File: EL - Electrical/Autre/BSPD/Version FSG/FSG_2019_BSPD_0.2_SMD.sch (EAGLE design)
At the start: 49 parts, among them K101 CP1-12V, T101 Si2309CDS, T102 BSS138, T103 BSS138

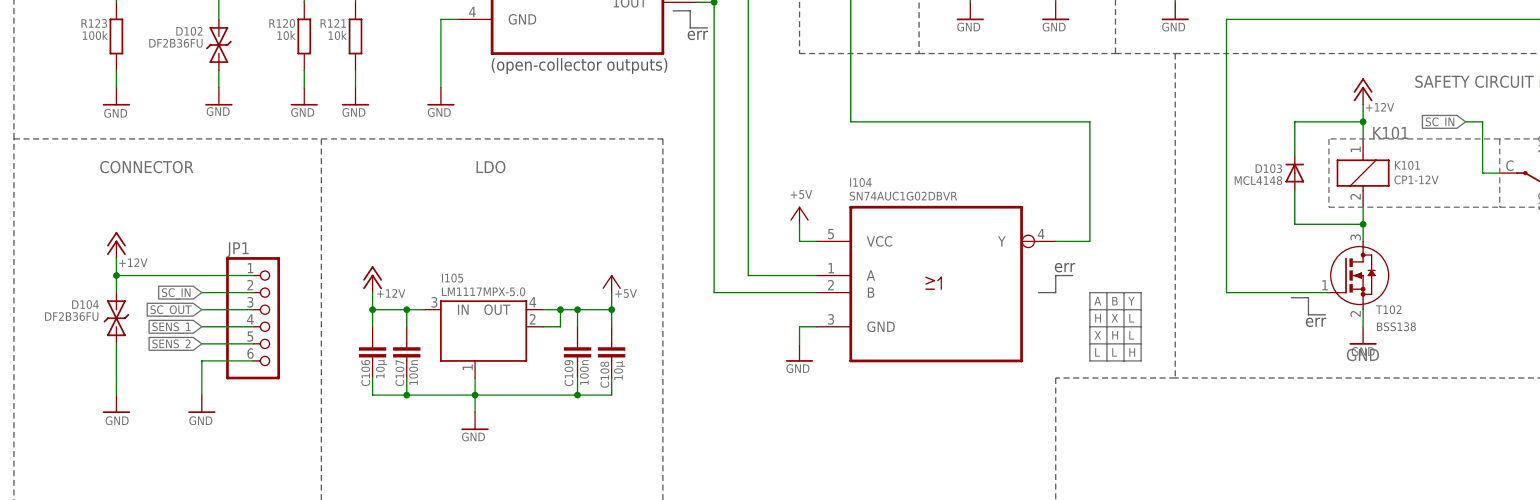
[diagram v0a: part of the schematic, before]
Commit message: Mofif connecteur BSPD
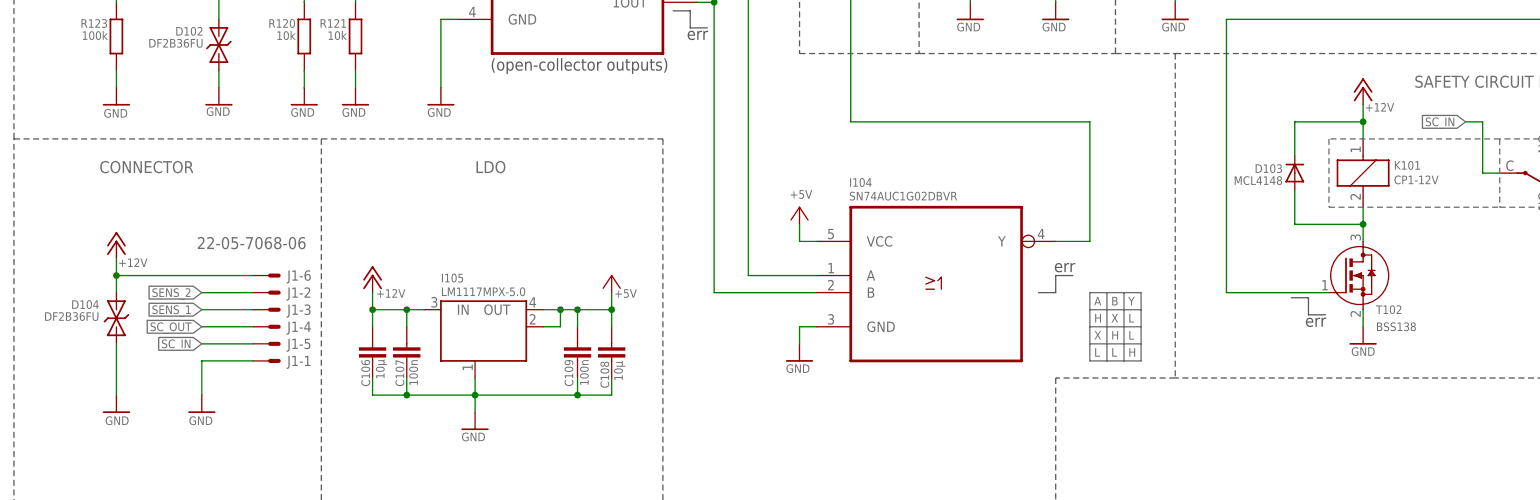
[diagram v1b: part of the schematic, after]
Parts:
- removed JP1: (no value), pinhead:PINHD-1X6
- added J1: 22-05-7068-06, con-molex:22-05-7068-06
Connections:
- net +12V: now also J1-6.S; no longer JP1.1
- net GND: now also J1-1.S; no longer JP1.6
- net SC_IN: now also J1-5.S; no longer JP1.2
- net SC_OUT: now also J1-4.S; no longer JP1.3
- net SENS_1: now also J1-3.S; no longer JP1.4
- net SENS_2: now also J1-2.S; no longer JP1.5
